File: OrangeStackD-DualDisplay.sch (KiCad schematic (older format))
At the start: 6 parts, among them J1 DISPLAY, J2 OrangePi, J3 DVMega, J4 GS3, J5 GS3, J6 PWR

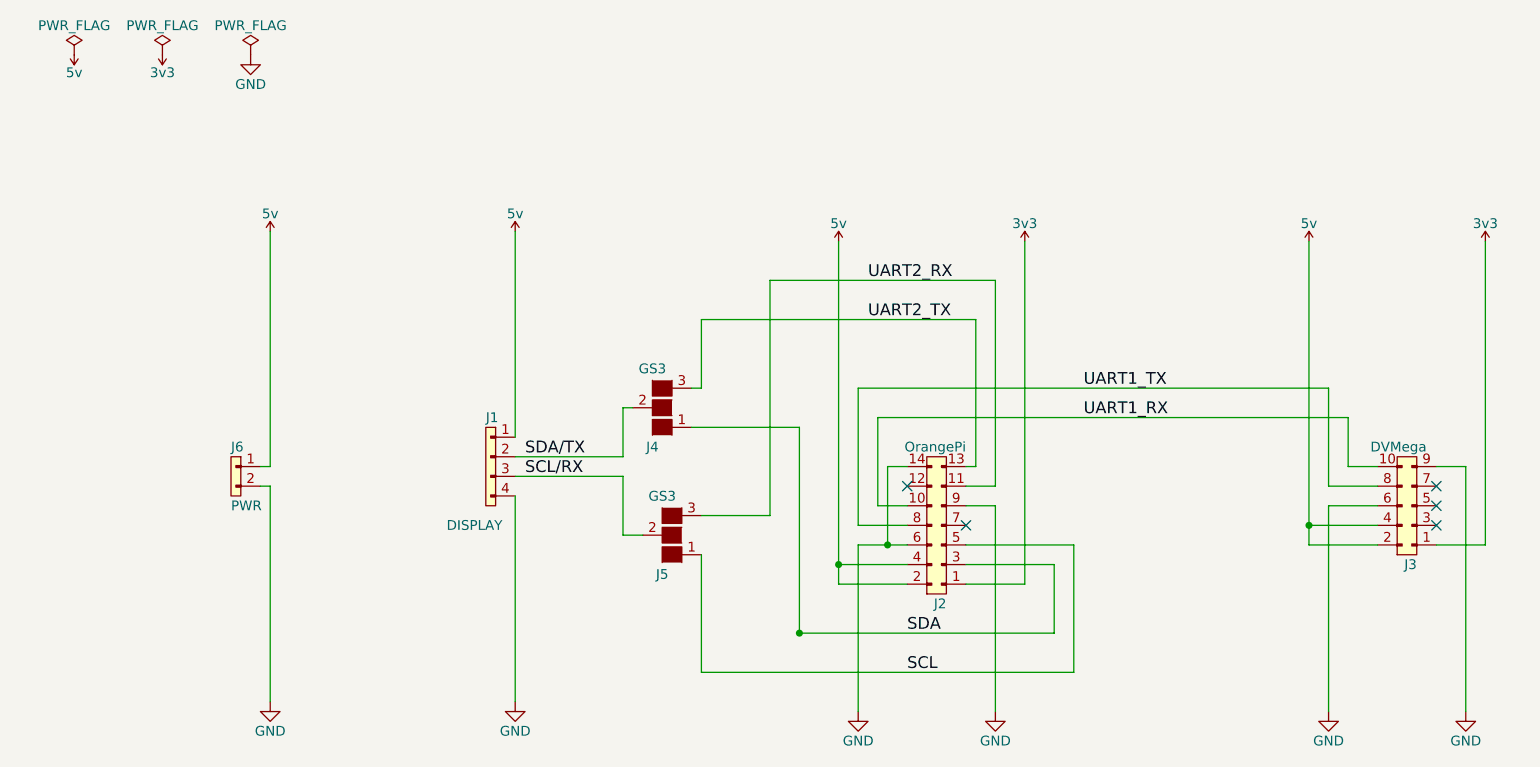
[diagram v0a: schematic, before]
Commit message: Fixes issue with DVMega connector, adds power filtering and safety features
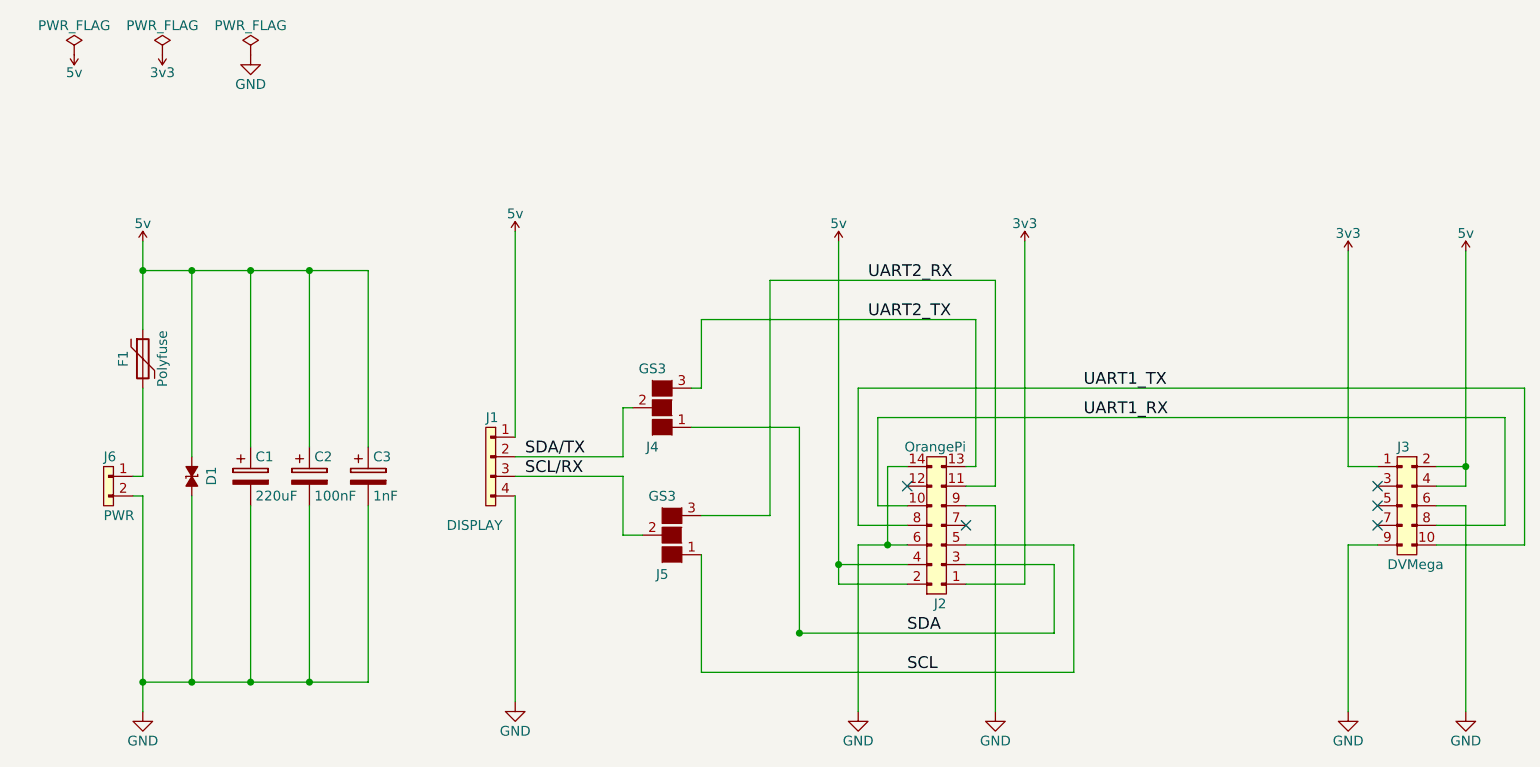
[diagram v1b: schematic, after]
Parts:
- added C1: 220uF, agg:1206, symbol CP
- added C2: 100nF, agg:0805, symbol CP
- added C3: 1nF, agg:0805, symbol CP
- added D1: ESD_DIODE, agg:DO-214AA-SMB, symbol ESD_DIODE
- added F1: Polyfuse, Fuse_Holders_and_Fuses:Fuse_SMD2920, symbol Polyfuse
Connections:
- net 5v: now also C1.1, C2.1, C3.1, D1.1, F1.1; no longer J6.1
- net GND: now also C1.2, C2.2, C3.2, D1.2
- net UART1_RX: now also J3.8; no longer J3.10
- net UART1_TX: now also J3.10; no longer J3.8
- new net: F1.2, J6.1
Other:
- moved on the sheet: J6

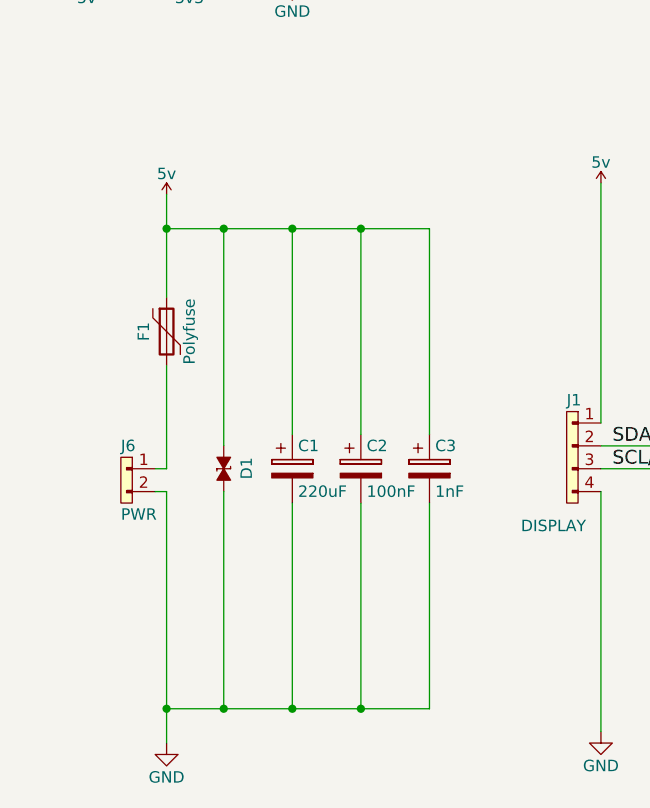
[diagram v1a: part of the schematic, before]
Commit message: Adds power LED
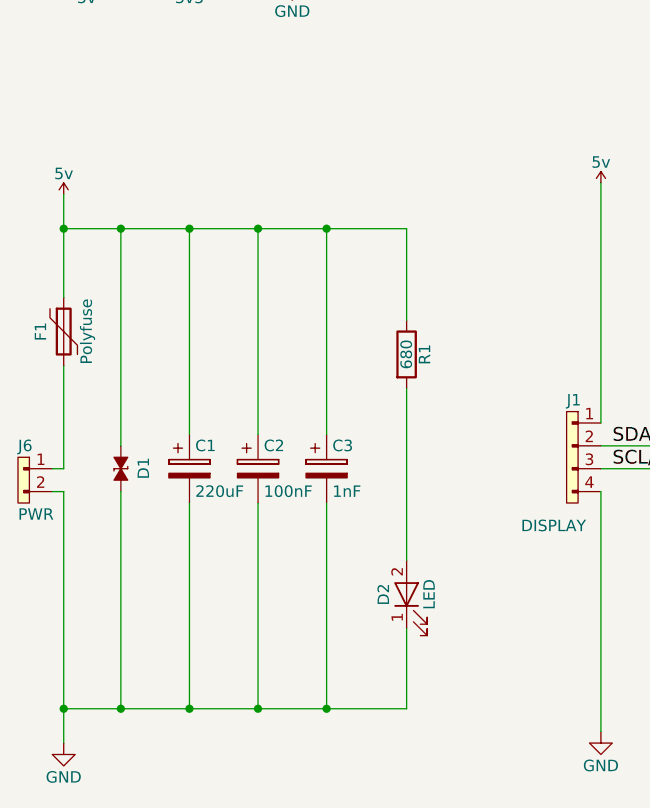
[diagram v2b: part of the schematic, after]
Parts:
- added D2: LED, agg:0805-LED, symbol LED
- added R1: 680, agg:0805, symbol R
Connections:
- net 5v: now also R1.1
- net GND: now also D2.1 (K)
- new net: D2.2 (A), R1.2
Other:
- moved on the sheet: C1, C2, C3, D1, F1, J6
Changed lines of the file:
@@
 L 5v #PWR015
 U 1 1 597E5C2C
-P 2650 2550
-F 0 "#PWR015" H 2650 2660 50  0001 L CNN
-F 1 "5v" H 2650 2640 50  0000 C CNN
-F 2 "" H 2650 2550 60  0001 C CNN
-F 3 "" H 2650 2550 60  0001 C CNN
-	1    2650 2550
+P 2200 2550
+F 0 "#PWR015" H 2200 2660 50  0001 L CNN
+F 1 "5v" H 2200 2640 50  0000 C CNN
+F 2 "" H 2200 2550 60  0001 C CNN
+F 3 "" H 2200 2550 60  0001 C CNN
+	1    2200 2550
 	1    0    0    -1
 $EndComp
@@
 L GND #PWR016
 U 1 1 597E5C49
-P 2650 4950
-F 0 "#PWR016" H 2650 4700 50  0001 C CNN
-F 1 "GND" H 2650 4800 50  0000 C CNN
-F 2 "" H 2650 4950 50  0001 C CNN
-F 3 "" H 2650 4950 50  0001 C CNN
-	1    2650 4950
+P 2200 4950
+F 0 "#PWR016" H 2200 4700 50  0001 C CNN
+F 1 "GND" H 2200 4800 50  0000 C CNN
+F 2 "" H 2200 4950 50  0001 C CNN
+F 3 "" H 2200 4950 50  0001 C CNN
+	1    2200 4950
 	1    0    0    -1
 $EndComp
@@
 L CONN_01x02 J6
 U 1 1 597E5C72
-P 2500 3750
-F 0 "J6" H 2450 3850 50  0000 L CNN
-F 1 "PWR" H 2450 3550 50  0000 L CNN
-F 2 "agg:SIL-254P-02" H 2500 3750 50  0001 C CNN
-F 3 "" H 2500 3750 50  0001 C CNN
-	1    2500 3750
+P 2050 3750
+F 0 "J6" H 2000 3850 50  0000 L CNN
+F 1 "PWR" H 2000 3550 50  0000 L CNN
+F 2 "agg:SIL-254P-02" H 2050 3750 50  0001 C CNN
+F 3 "" H 2050 3750 50  0001 C CNN
+	1    2050 3750
 	1    0    0    -1
 $EndComp
@@
 L Polyfuse F1
 U 1 1 59D14BF0
-P 2650 3150
-F 0 "F1" V 2550 3150 50  0000 C CNN
-F 1 "Polyfuse" V 2750 3150 50  0000 C CNN
-F 2 "Fuse_Holders_and_Fuses:Fuse_SMD2920" H 2700 2950 50  0001 L CNN
-F 3 "" H 2650 3150 50  0001 C CNN
-	1    2650 3150
+P 2200 3150
+F 0 "F1" V 2100 3150 50  0000 C CNN
+F 1 "Polyfuse" V 2300 3150 50  0000 C CNN
+F 2 "Fuse_Holders_and_Fuses:Fuse_SMD2920" H 2250 2950 50  0001 L CNN
+F 3 "" H 2200 3150 50  0001 C CNN
+	1    2200 3150
 	1    0    0    -1
 $EndComp
@@
 L CP C1
 U 1 1 59D33ABA
-P 3200 3750
-F 0 "C1" H 3225 3850 50  0000 L CNN
-F 1 "220uF" H 3225 3650 50  0000 L CNN
-F 2 "agg:1206" H 3238 3600 50  0001 C CNN
-F 3 "" H 3200 3750 50  0001 C CNN
-	1    3200 3750
+P 2750 3750
+F 0 "C1" H 2775 3850 50  0000 L CNN
+F 1 "220uF" H 2775 3650 50  0000 L CNN
+F 2 "agg:1206" H 2788 3600 50  0001 C CNN
+F 3 "" H 2750 3750 50  0001 C CNN
+	1    2750 3750
 	1    0    0    -1
 $EndComp
@@
 L CP C2
 U 1 1 59D33B5E
-P 3500 3750
-F 0 "C2" H 3525 3850 50  0000 L CNN
-F 1 "100nF" H 3525 3650 50  0000 L CNN
-F 2 "agg:0805" H 3538 3600 50  0001 C CNN
-F 3 "" H 3500 3750 50  0001 C CNN
-	1    3500 3750
+P 3050 3750
+F 0 "C2" H 3075 3850 50  0000 L CNN
+F 1 "100nF" H 3075 3650 50  0000 L CNN
+F 2 "agg:0805" H 3088 3600 50  0001 C CNN
+F 3 "" H 3050 3750 50  0001 C CNN
+	1    3050 3750
 	1    0    0    -1
 $EndComp
@@
 L CP C3
 U 1 1 59D33BB0
-P 3800 3750
-F 0 "C3" H 3825 3850 50  0000 L CNN
-F 1 "1nF" H 3825 3650 50  0000 L CNN
-F 2 "agg:0805" H 3838 3600 50  0001 C CNN
-F 3 "" H 3800 3750 50  0001 C CNN
-	1    3800 3750
+P 3350 3750
+F 0 "C3" H 3375 3850 50  0000 L CNN
+F 1 "1nF" H 3375 3650 50  0000 L CNN
+F 2 "agg:0805" H 3388 3600 50  0001 C CNN
+F 3 "" H 3350 3750 50  0001 C CNN
+	1    3350 3750
 	1    0    0    -1
 $EndComp
@@
 L ESD_DIODE D1
 U 1 1 59D33C0D
-P 2900 3750
-F 0 "D1" H 2850 3850 50  0000 L CNN
-F 1 "ESD_DIODE" H 2850 3650 50  0001 L CNN
-F 2 "agg:DO-214AA-SMB" H 2850 3550 50  0001 L CNN
-F 3 "" H 2800 3750 50  0001 C CNN
-F 4 "2368169" H 2850 3450 50  0001 L CNN "Farnell"
-	1    2900 3750
+P 2450 3750
+F 0 "D1" H 2400 3850 50  0000 L CNN
+F 1 "ESD_DIODE" H 2400 3650 50  0001 L CNN
+F 2 "agg:DO-214AA-SMB" H 2400 3550 50  0001 L CNN
+F 3 "" H 2350 3750 50  0001 C CNN
+F 4 "2368169" H 2400 3450 50  0001 L CNN "Farnell"
+	1    2450 3750
 	0    1    1    0
 $EndComp
@@
 	5850 3950 5850 2750
 Wire Wire Line
-	2600 3750 2650 3750
-Wire Wire Line
-	2600 3850 2650 3850
-Wire Wire Line
-	2650 3850 2650 4950
+	2150 3750 2200 3750
+Wire Wire Line
+	2150 3850 2200 3850
+Wire Wire Line
+	2200 3850 2200 4950
 Wire Wire Line
 	6550 3900 6400 3900
@@
 	9400 3900 9400 4950
 Wire Wire Line
-	2650 2550 2650 3000
-Wire Wire Line
-	2650 3750 2650 3300
-Wire Wire Line
-	2650 2700 3800 2700
-Wire Wire Line
-	3800 2700 3800 3600
-Connection ~ 2650 2700
-Connection ~ 3500 2700
-Wire Wire Line
-	3200 3600 3200 2700
-Connection ~ 3200 2700
-Wire Wire Line
-	2900 3650 2900 2700
-Connection ~ 2900 2700
-Wire Wire Line
-	2900 3850 2900 4800
-Wire Wire Line
-	2650 4800 3800 4800
-Connection ~ 2650 4800
-Wire Wire Line
-	3200 4800 3200 3900
-Connection ~ 2900 4800
-Wire Wire Line
-	3500 4800 3500 3900
-Connection ~ 3200 4800
-Wire Wire Line
-	3800 4800 3800 3900
-Connection ~ 3500 4800
-Wire Wire Line
-	3500 3600 3500 2700
+	2200 2550 2200 3000
+Wire Wire Line
+	2200 3750 2200 3300
+Wire Wire Line
+	2200 2700 3700 2700
+Wire Wire Line
+	3350 2700 3350 3600
+Connection ~ 2200 2700
+Connection ~ 3050 2700
+Wire Wire Line
+	2750 3600 2750 2700
+Connection ~ 2750 2700
+Wire Wire Line
+	2450 3650 2450 2700
+Connection ~ 2450 2700
+Wire Wire Line
+	2450 3850 2450 4800
+Wire Wire Line
+	2200 4800 3700 4800
+Connection ~ 2200 4800
+Wire Wire Line
+	2750 4800 2750 3900
+Connection ~ 2450 4800
+Wire Wire Line
+	3050 4800 3050 3900
+Connection ~ 2750 4800
+Wire Wire Line
+	3350 4800 3350 3900
+Connection ~ 3050 4800
+Wire Wire Line
+	3050 3600 3050 2700
+$Comp
+L R R1
+U 1 1 59D40443
+P 3700 3250
+F 0 "R1" V 3780 3250 50  0000 C CNN
+F 1 "680" V 3700 3250 50  0000 C CNN
+F 2 "agg:0805" V 3630 3250 50  0001 C CNN
+F 3 "" H 3700 3250 50  0001 C CNN
+	1    3700 3250
+	1    0    0    -1
+$EndComp
+$Comp
+L LED D2
+U 1 1 59D404B5
+P 3700 4300
+F 0 "D2" H 3700 4400 50  0000 C CNN
+F 1 "LED" H 3700 4200 50  0000 C CNN
+F 2 "agg:0805-LED" H 3700 4300 50  0001 C CNN
+F 3 "" H 3700 4300 50  0001 C CNN
+	1    3700 4300
+	0    -1   -1   0
+$EndComp
+Wire Wire Line
+	3700 2700 3700 3100
+Connection ~ 3350 2700
+Wire Wire Line
+	3700 3400 3700 4150
+Wire Wire Line
+	3700 4800 3700 4450
+Connection ~ 3350 4800
 $EndSCHEMATC
